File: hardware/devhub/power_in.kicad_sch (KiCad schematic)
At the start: 22 parts, among them J1 USB-C PWR IN, U1 AP2112K-3.3

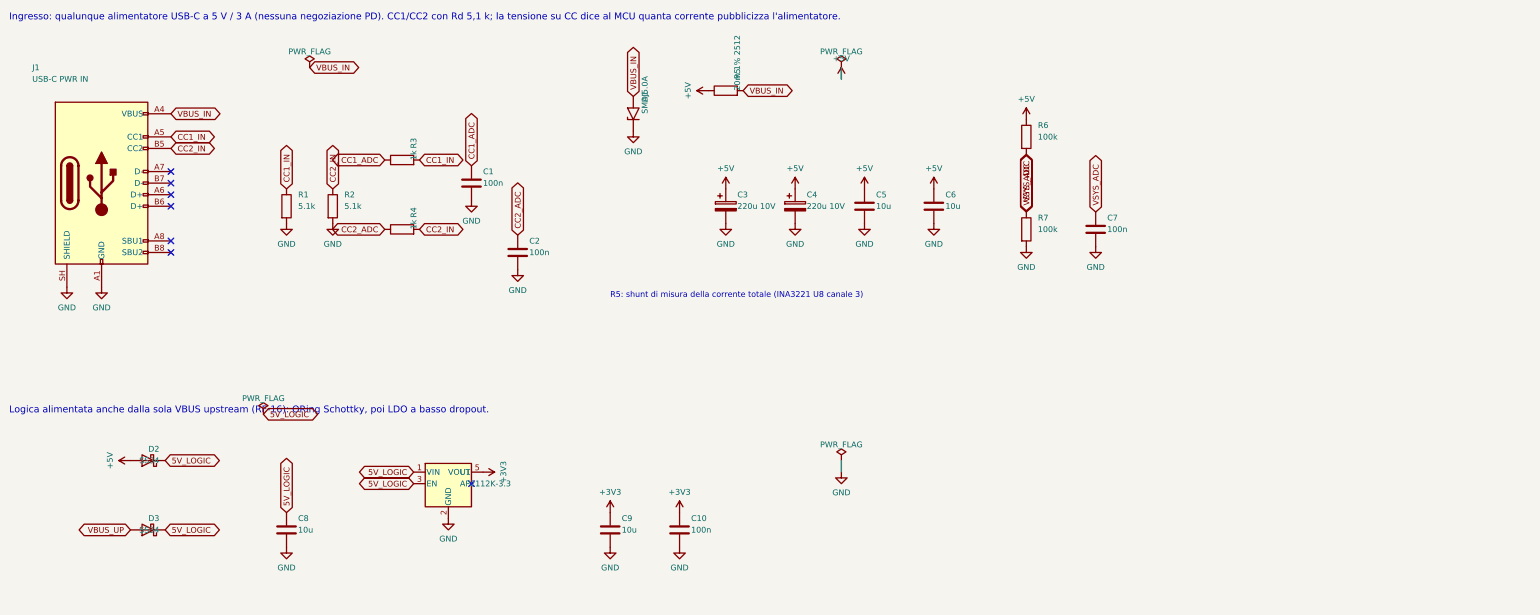
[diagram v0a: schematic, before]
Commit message: Schematic v0.2: hub reset supervisor, 1 A LDO, reorganized sheets, USB connectors and crystal
Functional changes:
- USB2517 RESET_N with pull-up and MCP120T-300 supervisor, wired-OR with
  the MCU (open-drain): resetting the MCU no longer resets the hub, so the
  ST DFU bootloader is reachable through it (D16/D17).
- 3.3 V LDO: AP7361C-33E (1 A, SOT-223) instead of AP2112K, which
  dissipated too much with the hub load.
- 74HC595 /OE on PB6 with pull-up: LEDs off until firmware enables them.
- Orange D93 instead of blue, USB-A bulk capacitance >= 120 uF, relay coil
  pinout fixed, snubbers marked DNP, Cliff FCR7350 banana jack footprints.
- D18: horizontal USB connectors, GCT USB4105-GF-A (USB-C) and Kycon
  KUSBX-AS1N-B (USB-A).
- D19: YXC X322524MOB4SI 24 MHz crystal (C_L 12 pF), 15 pF C0G load caps.

Layout: nearby parts wired directly, every net still explicitly named;
local labels inside sheets, global only across sheets, hierarchical for
ports. Files saved with KiCad 10.

Connectivity checked against the previous netlist, ERC clean.
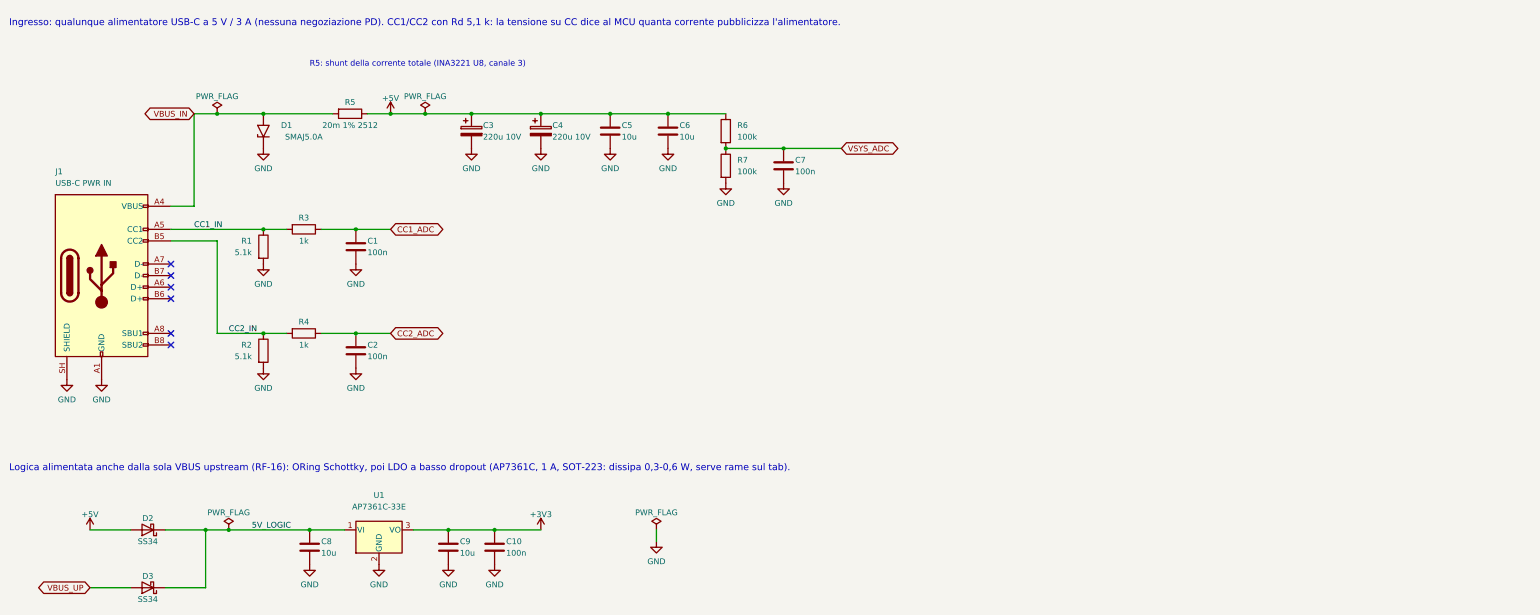
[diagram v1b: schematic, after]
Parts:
- removed U1: AP2112K-3.3, Package_TO_SOT_SMD:SOT-23-5, symbol Regulator_Linear:AP2112K-3.3
- added U1: AP7361C-33E, Package_TO_SOT_SMD:SOT-223-3_TabPin2, symbol Regulator_Linear:AP7361C-33E
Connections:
- net +3V3: now also U1.3 (VO)
- net 5V_LOGIC: now also U1.1 (VI)
- net GND: now also U1.2 (GND)
- no-connect marks 7 -> 6
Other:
- note added: "Ingresso: qualunque alimentatore USB-C a 5 V / 3 A (nessuna negoziazione PD). CC1/CC2 con Rd 5,1 k: la tensione su CC dice al MCU quanta corrente pubblicizza l'alimentatore."
- note added: "Logica alimentata anche dalla sola VBUS upstream (RF-16): ORing Schottky, poi LDO a basso dropout (AP7361C, 1 A, SOT-223: dissipa 0,3-0,6 W, serve rame sul tab)."
- note added: "R5: shunt della corrente totale (INA3221 U8, canale 3)"
- note removed: "Ingresso: qualunque alimentatore USB-C a 5 V / 3 A (nessuna negoziazione PD). CC1/CC2 con Rd 5,1 k; la tensione su CC dice al MCU quanta corrente pubblicizza l'alimentatore."
- note removed: "Logica alimentata anche dalla sola VBUS upstream (RF-16): ORing Schottky, poi LDO a basso dropout."
- note removed: "R5: shunt di misura della corrente totale (INA3221 U8 canale 3)"

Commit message: Lab-use protection: TPS259470A input eFuse, PI3USB4002A data switches; AGENTS.md
Power input (D20, D21):
- TPS259470A eFuse after the shunt: trips above 5.84 V and below 4.0 V,
  zener on EN to withstand up to 28 V, 3.5 A limit, ~5 ms soft start,
  auto-retry, FLT to the MCU on PB1.
- The shunt stays before the eFuse, so the INA3221 still measures the input
  voltage when the eFuse is off.

Ports (D22): PI3USB4002A instead of TS3USB30E. The connector side withstands
24 V and opens above 4.75 V, so a D+/D- short to VBUS on a board under test
no longer reaches the 3.3 V rail.

Symbols for both ICs added to the project library. AGENTS.md added: the
schematic is edited in KiCad or with targeted changes, never regenerated by
script. Sheets re-saved by KiCad.

Connectivity checked against the previous netlist, ERC clean.
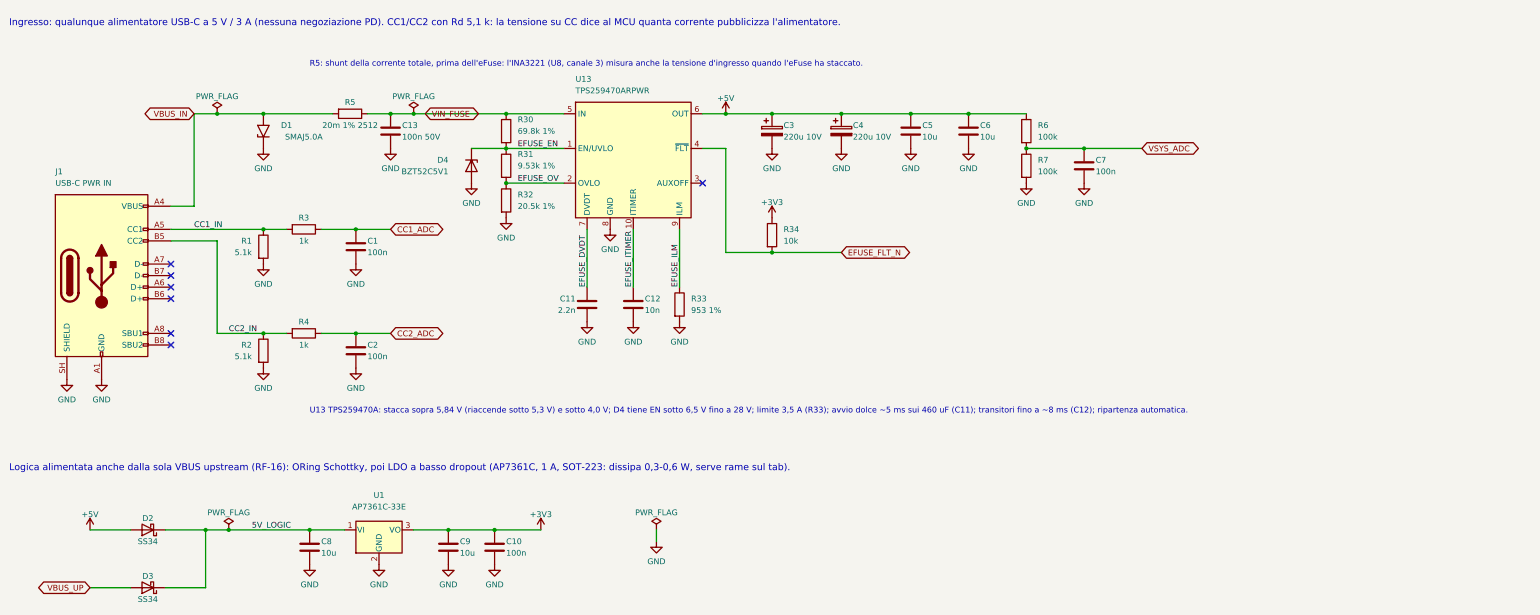
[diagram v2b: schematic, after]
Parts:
- added C11: 2.2n, Capacitor_SMD:C_0603_1608Metric, symbol Device:C
- added C12: 10n, Capacitor_SMD:C_0603_1608Metric, symbol Device:C
- added C13: 100n 50V, Capacitor_SMD:C_0603_1608Metric, symbol Device:C
- added D4: BZT52C5V1, Diode_SMD:D_SOD-123, symbol Device:D_Zener
- added R30: 69.8k 1%, Resistor_SMD:R_0603_1608Metric, symbol Device:R
- added R31: 9.53k 1%, Resistor_SMD:R_0603_1608Metric, symbol Device:R
- added R32: 20.5k 1%, Resistor_SMD:R_0603_1608Metric, symbol Device:R
- added R33: 953 1%, Resistor_SMD:R_0603_1608Metric, symbol Device:R
- added R34: 10k, Resistor_SMD:R_0603_1608Metric, symbol Device:R
- added U13: TPS259470ARPWR, symbol devhub:TPS259470A
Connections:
- net +3V3: now also R34.1
- net +5V: now also U13.6 (OUT); no longer R5.1
- net GND: now also C11.2, C12.2, C13.2, D4.2 (A), R32.2, R33.2, U13.8 (GND)
- new net EFUSE_DVDT: C11.1, U13.7 (DVDT)
- new net EFUSE_EN: D4.1 (K), R30.2, R31.1, U13.1 (EN/UVLO)
- new net EFUSE_FLT_N: R34.2, U13.4 (~{FLT})
- new net EFUSE_ILM: R33.1, U13.9 (ILM)
- new net EFUSE_ITIMER: C12.1, U13.10 (ITIMER)
- new net EFUSE_OV: R31.2, R32.1, U13.2 (OVLO)
- new net VIN_FUSE: C13.1, R30.1, R5.1, U13.5 (IN)
- no-connect marks 6 -> 7
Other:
- note added: "R5: shunt della corrente totale, prima dell'eFuse: l'INA3221 (U8, canale 3) misura anche la tensione d'ingresso quando l'eFuse ha staccato."
- note added: "U13 TPS259470A: stacca sopra 5,84 V (riaccende sotto 5,3 V) e sotto 4,0 V; D4 tiene EN sotto 6,5 V fino a 28 V; limite 3,5 A (R33); avvio dolce ~5 ms sui 460 uF (C11); transitori fino a ~8 ms (C12); ripartenza automatica."
- note removed: "R5: shunt della corrente totale (INA3221 U8, canale 3)"
- title: Alimentazione: ingresso USB-C 5 V, ORing e 3,3 V -> Alimentazione: ingresso USB-C 5 V, eFuse, ORing e 3,3 V
- moved on the sheet: C3, C4, C5, C6, C7, R6, R7

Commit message: SMAJ20A input TVS, no TVS on ports (D24, D25); relay push buttons (D26)
- The SMAJ5.0A already conducted at ~6.4 V and would burn with a 12-20 V
  supply before the eFuse trips; the SMAJ20A lets the eFuse do its job.
  No TVS on ports: it does not help against a sustained back-fed voltage.
  Two LEDs per port confirmed.
- SW1/SW2 on PB12/PB13 toggle the relays; new requirement RF-17 on panel
  buttons, RELAY_CHANGED event in the protocol.

Targeted schematic changes, connectivity otherwise unchanged, ERC clean.
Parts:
- D1: value SMAJ5.0A -> SMAJ20A; symbol Diode:SMAJ5.0A -> Diode:SMAJ20A
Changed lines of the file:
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@@
 	)
 	(symbol
-		(lib_id "Diode:SMAJ5.0A")
+		(lib_id "Diode:SMAJ20A")
 		(at 66.04 39.37 90)
 		(unit 1)
@@
 			)
 		)
-		(property "Value" "SMAJ5.0A"
+		(property "Value" "SMAJ20A"
 			(at 74.93 40.64 90)
 			(show_name no)
@@
 			)
 		)
-		(property "Description" "400W unidirectional Transient Voltage Suppressor, 5.0Vr, SMA(DO-214AC)"
+		(property "Description" "400W unidirectional Transient Voltage Suppressor, 20.0Vr, SMA(DO-214AC)"
 			(at 66.04 39.37 0)
 			(hide yes)

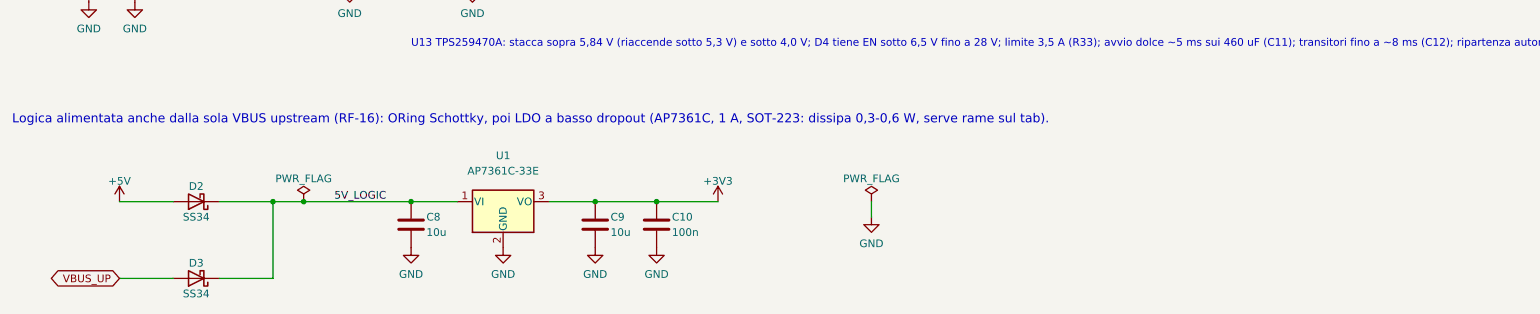
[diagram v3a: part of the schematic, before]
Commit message: Review 02, R02-05: drop RF-16, logic powered from the supply only (D32)
Removed D3; VBUS_DET and VSYS_ADC moved to 5 V tolerant pins (PA6, PA7).
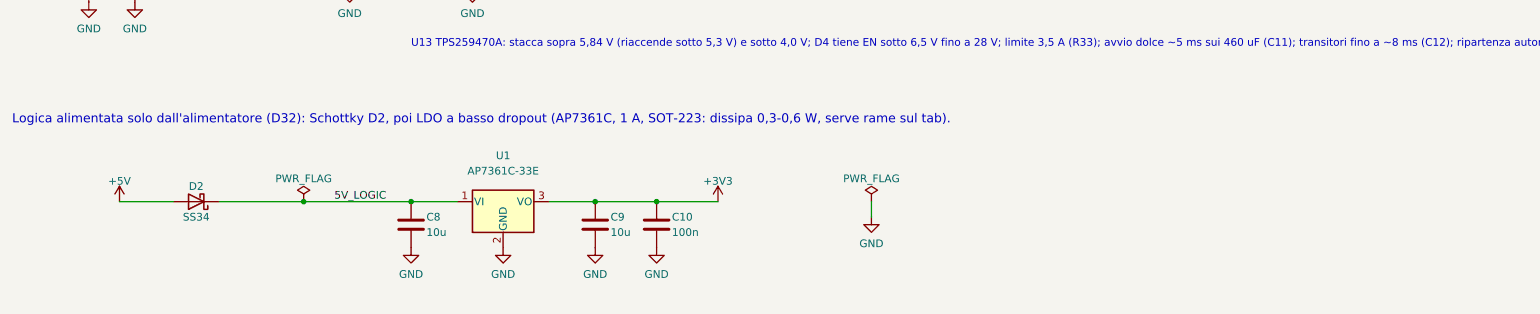
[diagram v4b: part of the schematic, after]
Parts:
- removed D3: SS34, Diode_SMD:D_SMA, symbol Device:D_Schottky
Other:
- note added: "Logica alimentata solo dall'alimentatore (D32): Schottky D2, poi LDO a basso dropout (AP7361C, 1 A, SOT-223: dissipa 0,3-0,6 W, serve rame sul tab)."
- note removed: "Logica alimentata anche dalla sola VBUS upstream (RF-16): ORing Schottky, poi LDO a basso dropout (AP7361C, 1 A, SOT-223: dissipa 0,3-0,6 W, serve rame sul tab)."
- title: Alimentazione: ingresso USB-C 5 V, eFuse, ORing e 3,3 V -> Alimentazione: ingresso USB-C 5 V, eFuse e 3,3 V
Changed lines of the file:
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@@
 	(paper "A3")
 	(title_block
-		(title "Alimentazione: ingresso USB-C 5 V, eFuse, ORing e 3,3 V")
+		(title "Alimentazione: ingresso USB-C 5 V, eFuse e 3,3 V")
 		(date "2026-10-10")
 		(rev "0.2")
@@
 		)
 	)
-	(text "Logica alimentata anche dalla sola VBUS upstream (RF-16): ORing Schottky, poi LDO a basso dropout (AP7361C, 1 A, SOT-223: dissipa 0,3-0,6 W, serve rame sul tab)."
+	(text "Logica alimentata solo dall'alimentatore (D32): Schottky D2, poi LDO a basso dropout (AP7361C, 1 A, SOT-223: dissipa 0,3-0,6 W, serve rame sul tab)."
 		(exclude_from_sim no)
 		(at 10.16 114.3 0)
@@
 	)
 	(junction
-		(at 53.34 127)
-		(diameter 0)
-		(color 0 0 0 0)
-	)
-	(junction
 		(at 58.42 127)
 		(diameter 0)
@@
 	(wire
 		(pts
-			(xy 53.34 139.7) (xy 53.34 127)
-		)
-		(stroke
-			(width 0)
-			(type default)
-		)
-	)
-	(wire
-		(pts
-			(xy 44.45 139.7) (xy 53.34 139.7)
-		)
-		(stroke
-			(width 0)
-			(type default)
-		)
-	)
-	(wire
-		(pts
 			(xy 99.06 127) (xy 106.68 127)
 		)
@@
 	(wire
 		(pts
-			(xy 27.94 139.7) (xy 36.83 139.7)
-		)
-		(stroke
-			(width 0)
-			(type default)
-		)
-	)
-	(wire
-		(pts
 			(xy 220.98 35.56) (xy 233.68 35.56)
 		)
@@
 		)
 	)
-	(global_label "VBUS_UP"
-		(shape bidirectional)
-		(at 27.94 139.7 180)
-		(fields_autoplaced yes)
-		(effects
-			(font
-				(size 1.27 1.27)
-			)
-			(justify right)
-		)
-		(property "Intersheetrefs" "${INTERSHEET_REFS}"
-			(at 27.94 139.7 0)
-			(hide yes)
-			(show_name no)
-			(do_not_autoplace no)
-			(effects
-				(font
-					(size 1.27 1.27)
-				)
-			)
-		)
-	)
 	(global_label "VIN_FUSE"
 		(shape bidirectional)
@@
 					(unit 1)
 				)
-			)
-		)
-	)
-	(symbol
-		(lib_id "Device:D_Schottky")
-		(at 40.64 139.7 180)
-		(unit 1)
-		(body_style 1)
-		(exclude_from_sim no)
-		(in_bom yes)
-		(on_board yes)
-		(in_pos_files yes)
-		(dnp no)
-		(property "Reference" "D3"
-			(at 40.64 137.16 0)
-			(show_name no)
-			(do_not_autoplace no)
-			(effects
-				(font
-					(size 1.27 1.27)
-				)
-			)
-		)
-		(property "Value" "SS34"
-			(at 40.64 142.24 0)
-			(show_name no)
-			(do_not_autoplace no)
-			(effects
-				(font
-					(size 1.27 1.27)
-				)
-			)
-		)
-		(property "Footprint" "Diode_SMD:D_SMA"
-			(at 40.64 139.7 0)
-			(hide yes)
-			(show_name no)
-			(do_not_autoplace no)
-			(effects
-				(font
-					(size 1.27 1.27)
-				)
-			)
-		)
-		(property "Datasheet" ""
-			(at 40.64 139.7 0)
-			(hide yes)
-			(show_name no)
-			(do_not_autoplace no)
-			(effects
-				(font
-					(size 1.27 1.27)
-				)
-			)
-		)
-		(property "Description" "Schottky diode"
-			(at 40.64 139.7 0)
-			(hide yes)
-			(show_name no)
-			(do_not_autoplace no)
-			(effects
-				(font
-					(size 1.27 1.27)
-				)
-			)
-		)
-		(pin "1"
-		)
-		(pin "2"
-		)
-		(instances
-			(project "devhub"
-				(path "/af6ea7d8-d1ba-5fc6-aec8-abf514847630/b7f46cfa-45c0-5dbb-a84a-cdf89b878306"
-					(reference "D3")
-					(unit 1)
-				)
